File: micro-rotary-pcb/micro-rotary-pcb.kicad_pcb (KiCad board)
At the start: 2 copper layers, 12 parts, among them P1 speed, U1 L7805

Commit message: pcb
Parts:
- +12v: renamed from Power 12v
- GND: renamed from Power GND
- H12v: renamed from H 12v
- H5v: renamed from H 5v
- moved D5 9.95 mm to (60.0, 102.0)
- moved H5v 7.50 mm to (60.0, 85.0)
- moved H GND 5.00 mm to (60.0, 95.0)
- moved GND 4.95 mm to (60.0, 71.5)
- moved H12v 4.50 mm to (60.0, 80.0)
- moved +12v 2.45 mm to (60.1, 66.5)
- moved D6 1.55 mm to (60.0, 107.0)
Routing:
- net Net-(A1-VIN): track 13.2 -> 107.7 mm
- net Net-(A1-D6): track 0.00 -> 33.4 mm
- net Net-(A1-D5): track 0.00 -> 18.8 mm
- net Net-(U1-IN): track 25.6 -> 44.1 mm
- net Net-(A1-A0): track 48.1 -> 44.3 mm
- net Net-(A1-+5V): track 24.8 -> 22.9 mm
- added copper zone on F.Cu, net (none)

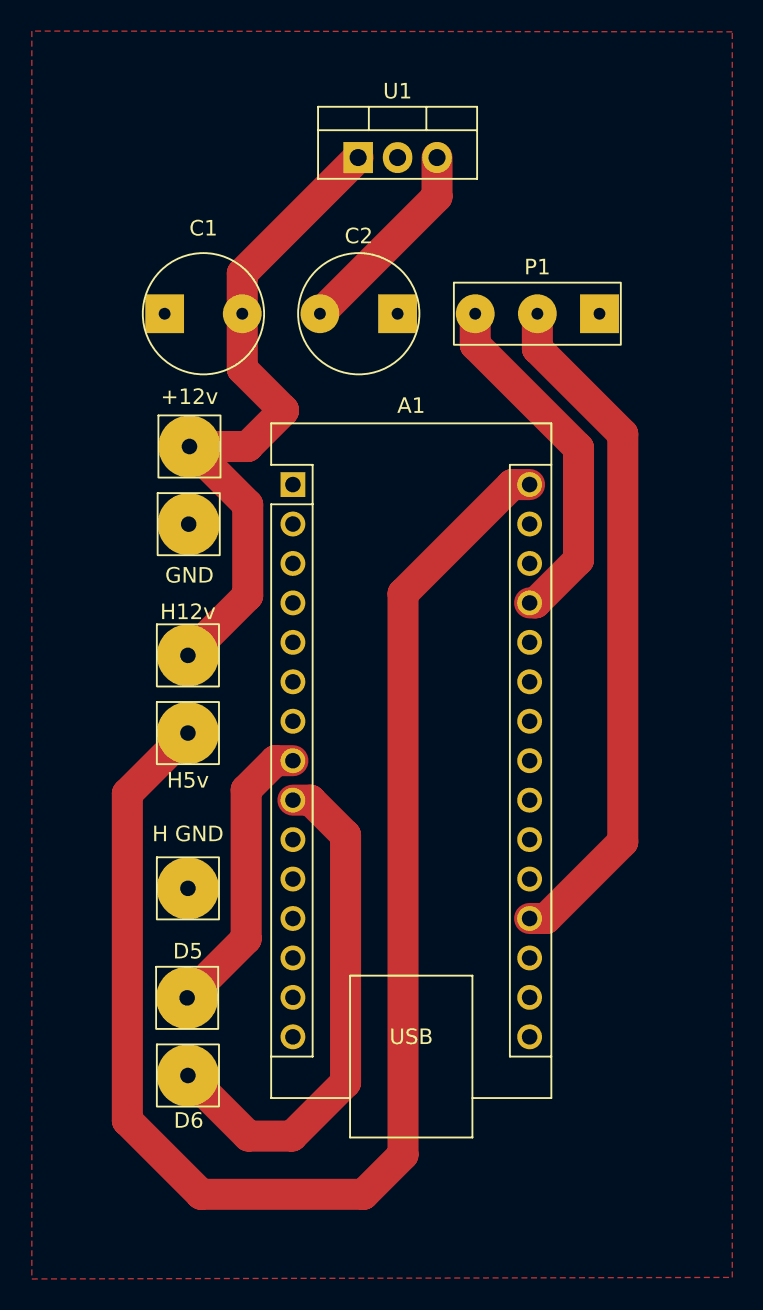
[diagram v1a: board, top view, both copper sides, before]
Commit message: fix vin
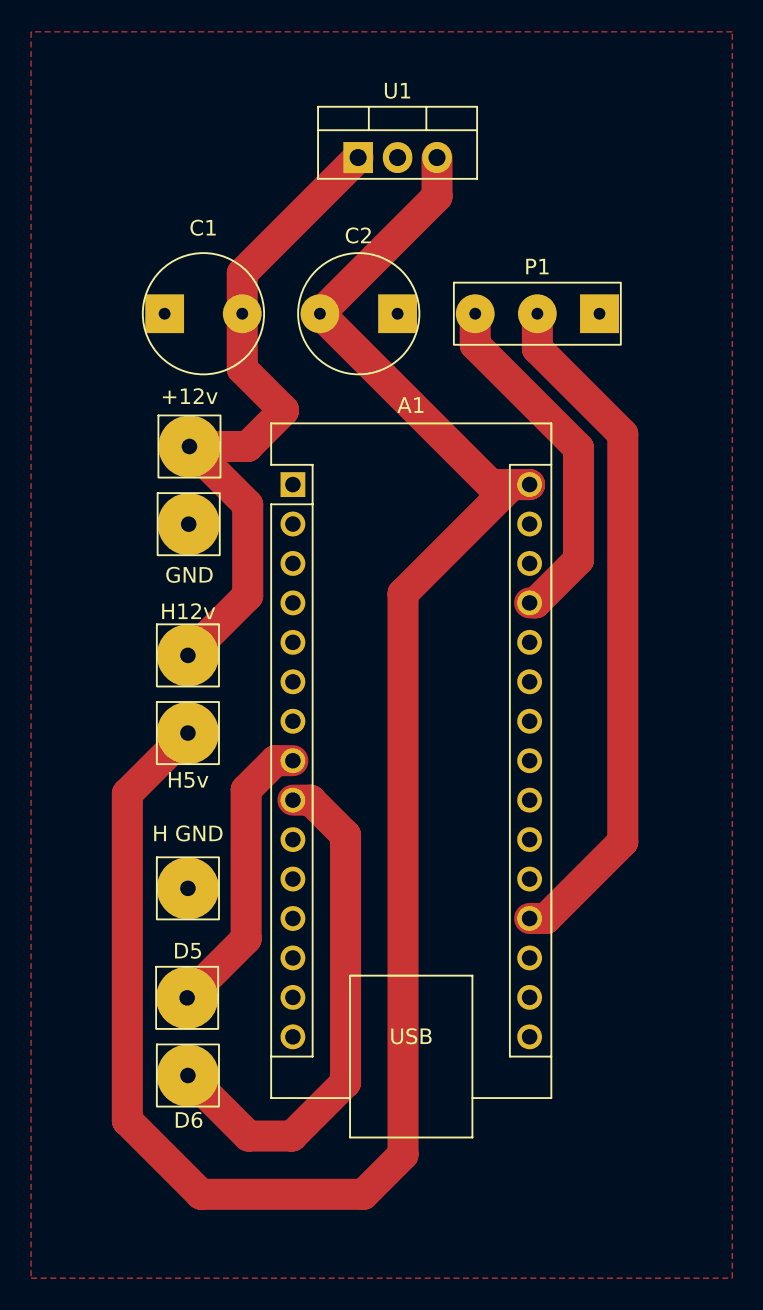
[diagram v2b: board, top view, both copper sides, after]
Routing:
- net Net-(A1-VIN): track 107.7 -> 125.8 mm
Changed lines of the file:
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@@
+	)
+	(segment
+		(start 79.5 69)
+		(end 82 69)
+		(width 2)
+		(layer "F.Cu")
+		(net 9)
 	)
 	(segment
@@
 		(start 73.85 76.01863)
 		(end 80.86863 69)
+		(width 2)
+		(layer "F.Cu")
+		(net 9)
+	)
+	(segment
+		(start 68.5 58)
+		(end 79.5 69)
 		(width 2)
 		(layer "F.Cu")
@@
 		(polygon
 			(pts
-				(xy 49.95 39.8) (xy 49.95 120.15) (xy 95.05 120.05) (xy 95.05 39.85)
+				(xy 49.9 39.85) (xy 49.9 120.1) (xy 95.05 120.1) (xy 95.05 39.85)
 			)
 		)

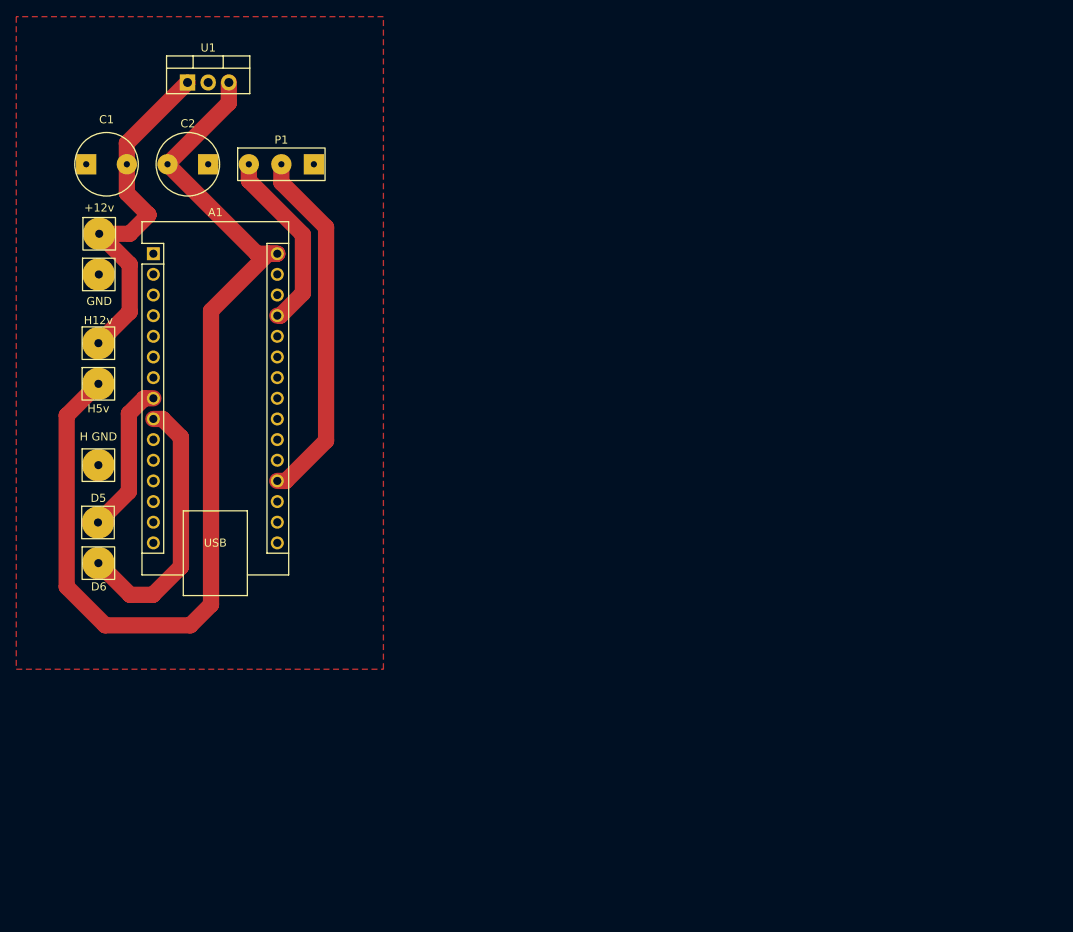
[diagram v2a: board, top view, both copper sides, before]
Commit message: fix gnd in pcb
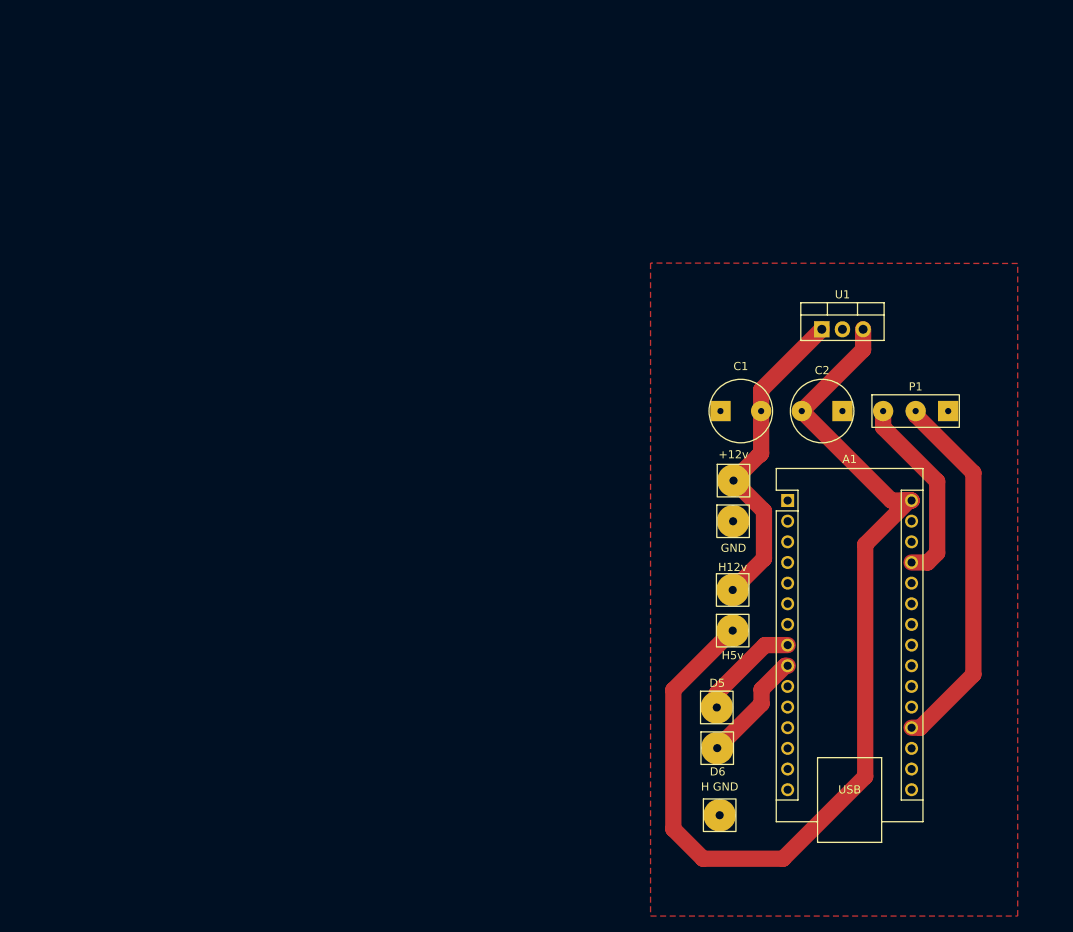
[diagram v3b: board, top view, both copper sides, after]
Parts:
- moved H GND 87.7 mm to (136.4, 138.1)
- moved GND 83.7 mm to (138.1, 101.9)
- moved U1 83.7 mm to (149.0, 78.3)
- moved +12v 83.7 mm to (138.1, 96.9)
- moved C1 83.7 mm to (139.0, 88.3)
- moved C2 83.7 mm to (149.0, 88.3)
- moved H12v 83.7 mm to (138.0, 110.3)
- moved H5v 83.7 mm to (138.0, 115.3)
- moved P1 83.7 mm to (160.5, 88.3)
- moved A1 83.7 mm to (144.8, 99.3)
- moved D5 79.4 mm to (136.1, 124.8)
- moved D6 79.4 mm to (136.1, 129.8)
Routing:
- net Net-(A1-D6): track 33.4 -> 13.9 mm
- net Net-(A1-D5): track 18.8 -> 12.9 mm
- net Net-(U1-IN): track 44.1 -> 39.7 mm
- net Net-(A1-A0): track 44.3 -> 45.6 mm
- net Net-(A1-+5V): track 22.9 -> 23.8 mm
- added copper zone on F.Cu, net GND
- removed copper zone on F.Cu, net (none)

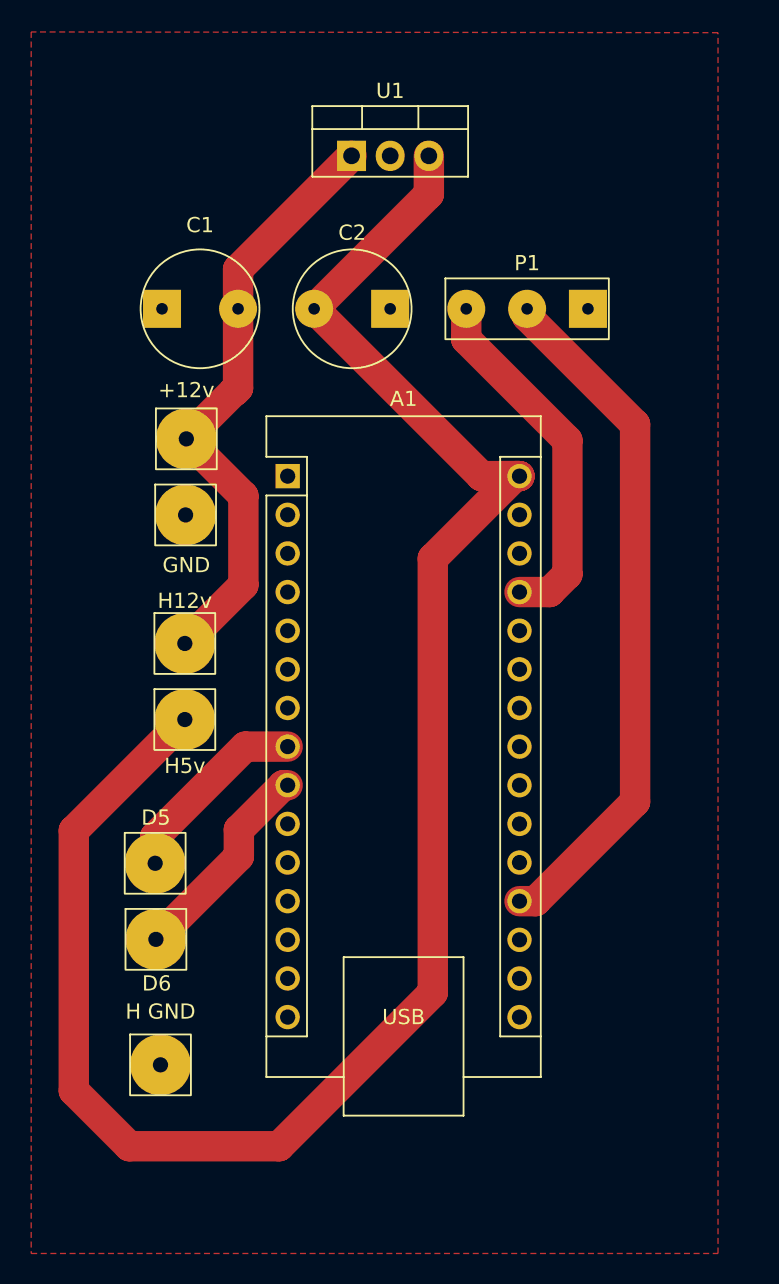
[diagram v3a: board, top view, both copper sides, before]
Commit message: change arduino e potentiometer footprint
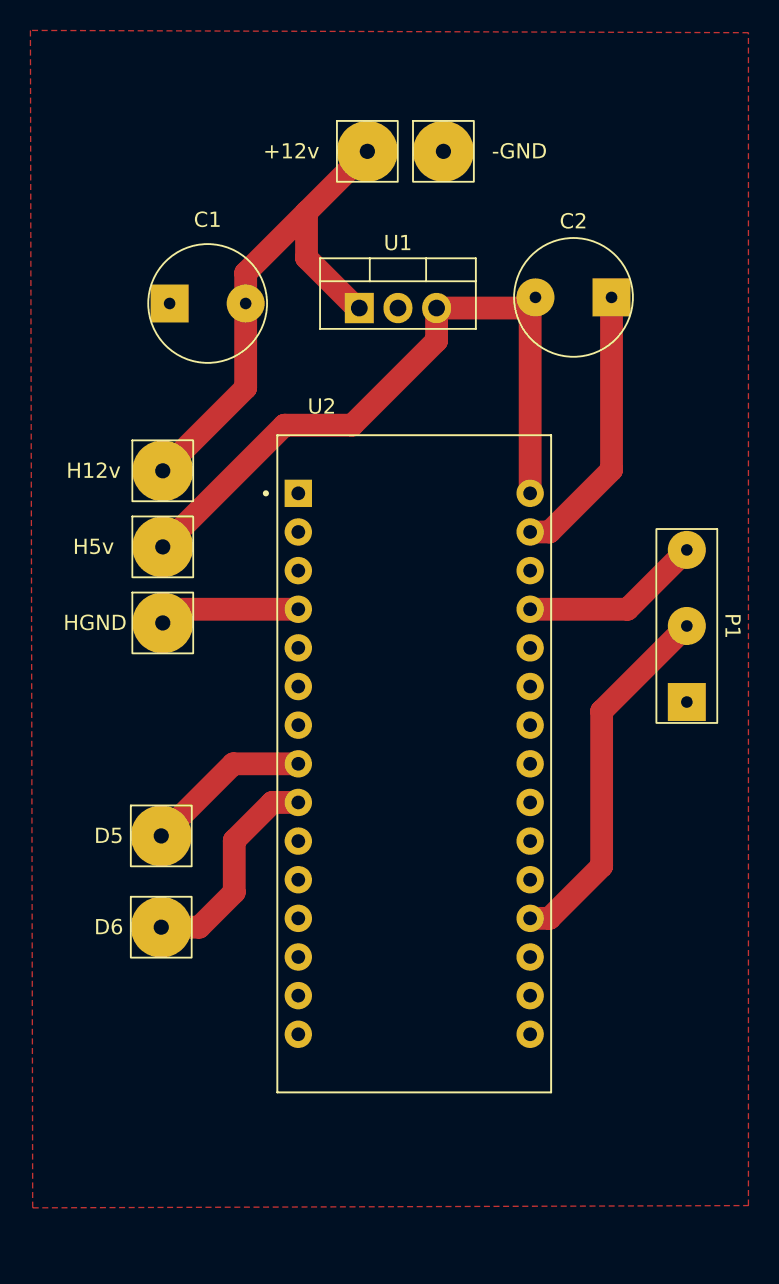
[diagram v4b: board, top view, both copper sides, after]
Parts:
- removed A1: Arduino_Nano_v3.x, Module:Arduino_Nano
- added U2: ARDUINO_NANO, Arduino:ARDUINO_NANO, F.Cu at (153.1, 118.3)
- HGND: renamed from H GND
- moved -GND 29.3 mm to (155.0, 78.0)
- moved HGND 29.1 mm to (136.6, 109.0)
- moved P1 23.3 mm to (171.0, 109.2), turned to -90 degrees
- moved +12v 22.3 mm to (150.0, 78.0)
- moved C2 14.6 mm to (163.6, 87.6)
- moved H12v 11.4 mm to (136.6, 99.0)
- moved H5v 11.4 mm to (136.6, 104.0)
- moved U1 10.0 mm to (149.5, 88.3)
- moved D5 1.84 mm to (136.4, 123.0)
- moved D6 0.87 mm to (136.4, 129.0)
- moved C1 0.61 mm to (139.5, 88.0)
- renumbered GND to -GND
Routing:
- net Net-(U1-OUT): track 125.6 -> 45.6 mm
- net GND: track 0.00 -> 27.7 mm
- net Net-(U2-A0): track 45.6 -> 24.2 mm
- net Net-(U2-+5V): track 23.8 -> 11.9 mm
- net Net-(U1-IN): track 39.7 -> 34.4 mm
- net Net-(U2-D5): track 12.9 -> 11.0 mm
- net Net-(U2-D6): track 13.9 -> 14.4 mm

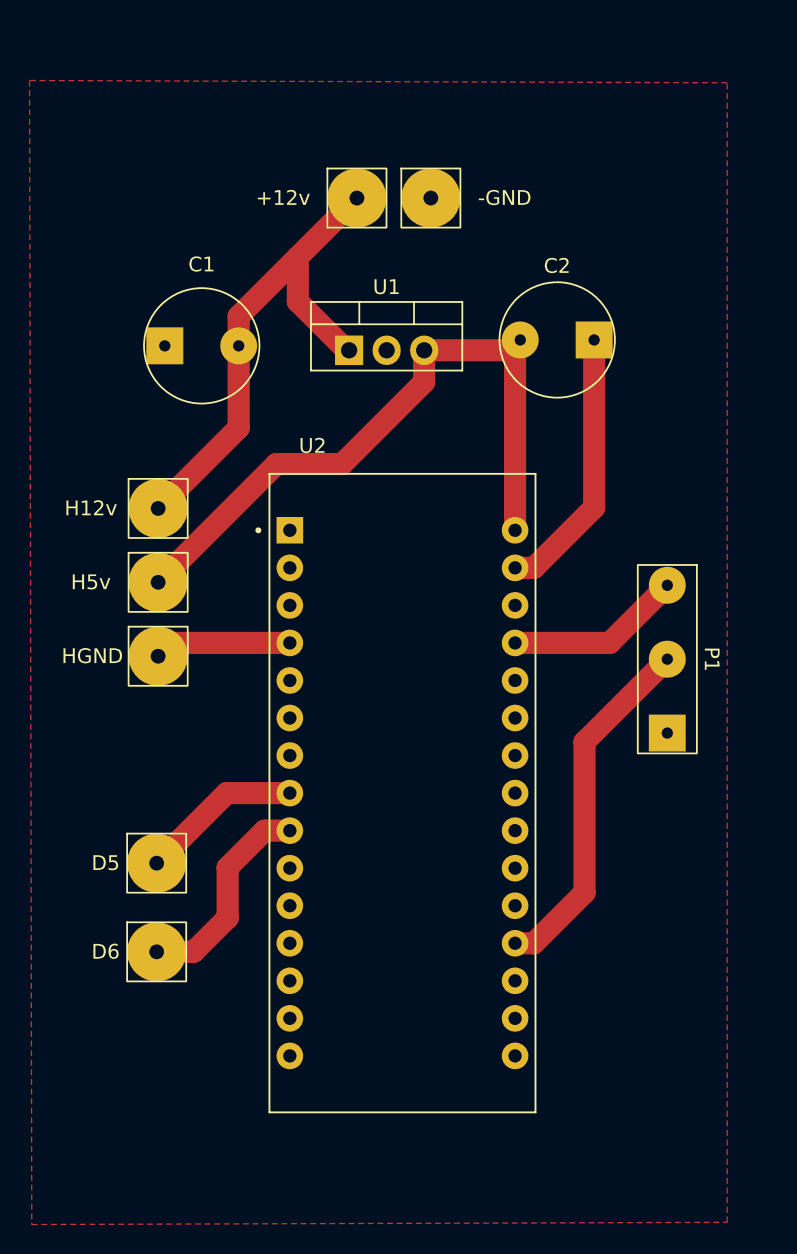
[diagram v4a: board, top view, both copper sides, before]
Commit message: fix inverted problem in pcb
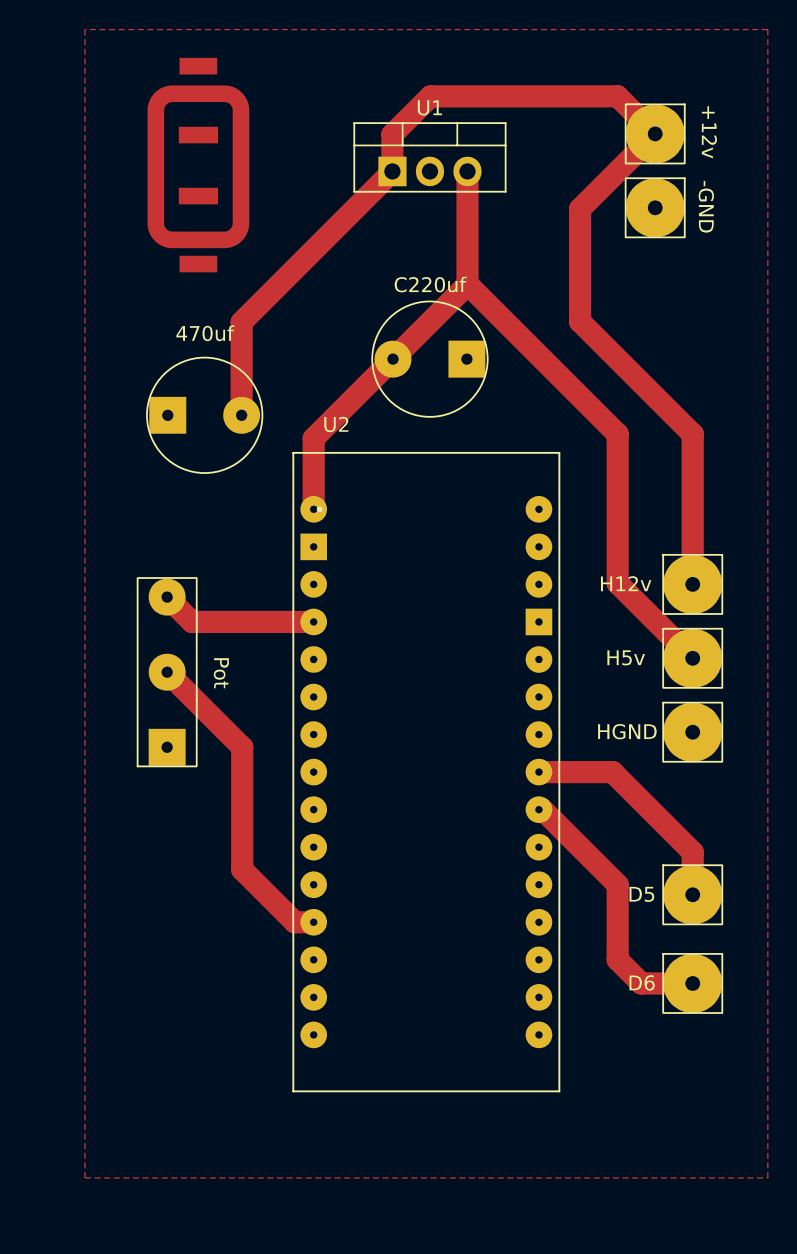
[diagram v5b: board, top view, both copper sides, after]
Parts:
- moved H12v 36.5 mm to (172.7, 104.1)
- moved H5v 36.5 mm to (172.7, 109.1)
- moved HGND 36.5 mm to (172.7, 114.1)
- moved D5 36.3 mm to (172.7, 125.1)
- moved D6 36.3 mm to (172.7, 131.1)
- moved Pot 33.9 mm to (137.2, 110.1), turned to 90 degrees
- moved +12v 20.6 mm to (170.2, 73.7), turned to -90 degrees
- moved -GND 15.2 mm to (170.2, 78.7), turned to -90 degrees
- moved U1 12.4 mm to (152.4, 76.2)
- moved C220uf 8.71 mm to (154.9, 88.9)
- moved 470uf 4.70 mm to (139.7, 92.7)
- moved U2 2.15 mm to (154.7, 116.8)
- renumbered C1 to 470uf, C2 to C220uf, P1 to Pot
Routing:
- net Net-(U1-IN): track 34.4 -> 78.9 mm
- net GND: track 27.7 -> 1.27 mm
- net Net-(U1-OUT): track 45.6 -> 58.8 mm
- net Net-(U2-D5): track 11.0 -> 15.5 mm
- net Net-(U2-D6): track 14.4 -> 18.3 mm
- net Net-(U2-A0): track 24.2 -> 21.8 mm
- net Net-(U2-+5V): track 11.9 -> 10.6 mm
